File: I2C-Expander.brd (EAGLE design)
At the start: 106 x 100 mm, 81 parts, among them IC1 MCP23017SO, IC2 PCA9555D, Q0 P-FET, Q1 P-FET, Q10 P-FET, Q11 P-FET, Q12 P-FET, Q13 P-FET, Q14 P-FET, Q15 P-FET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

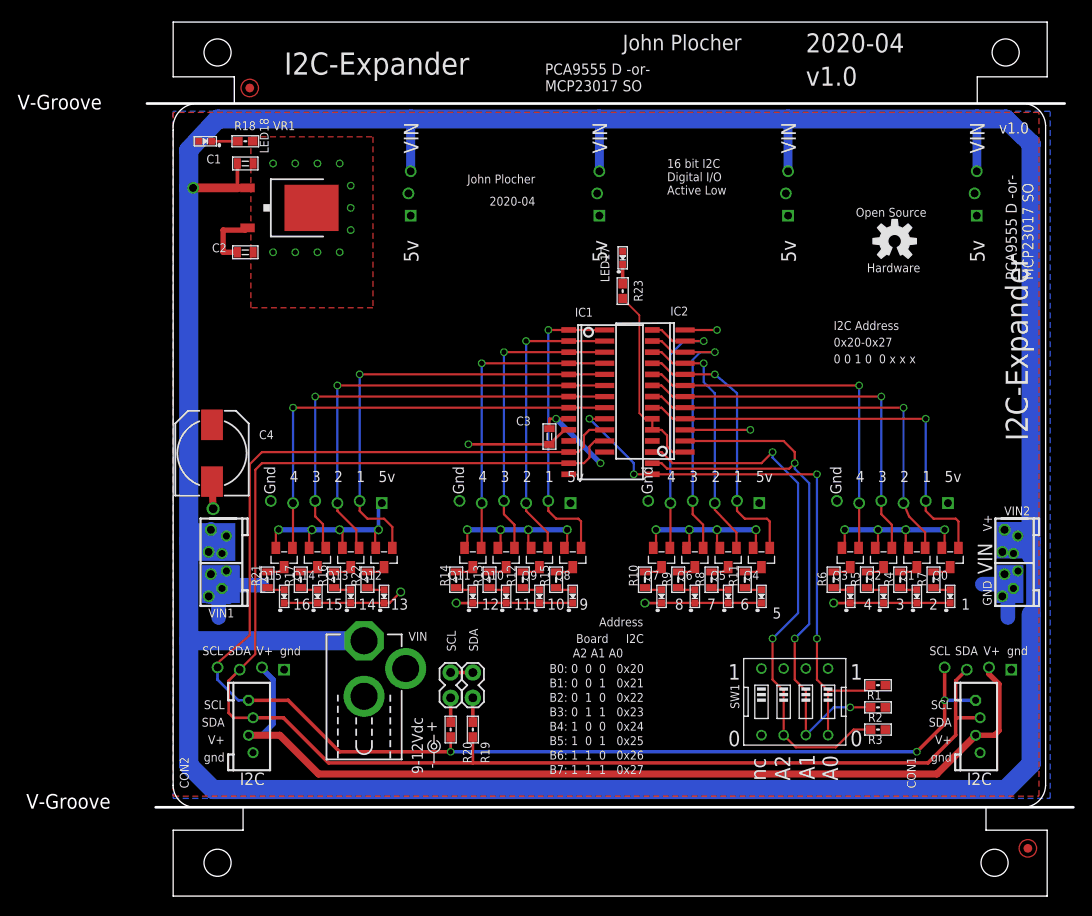
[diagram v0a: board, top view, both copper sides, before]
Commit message: FID placement & names
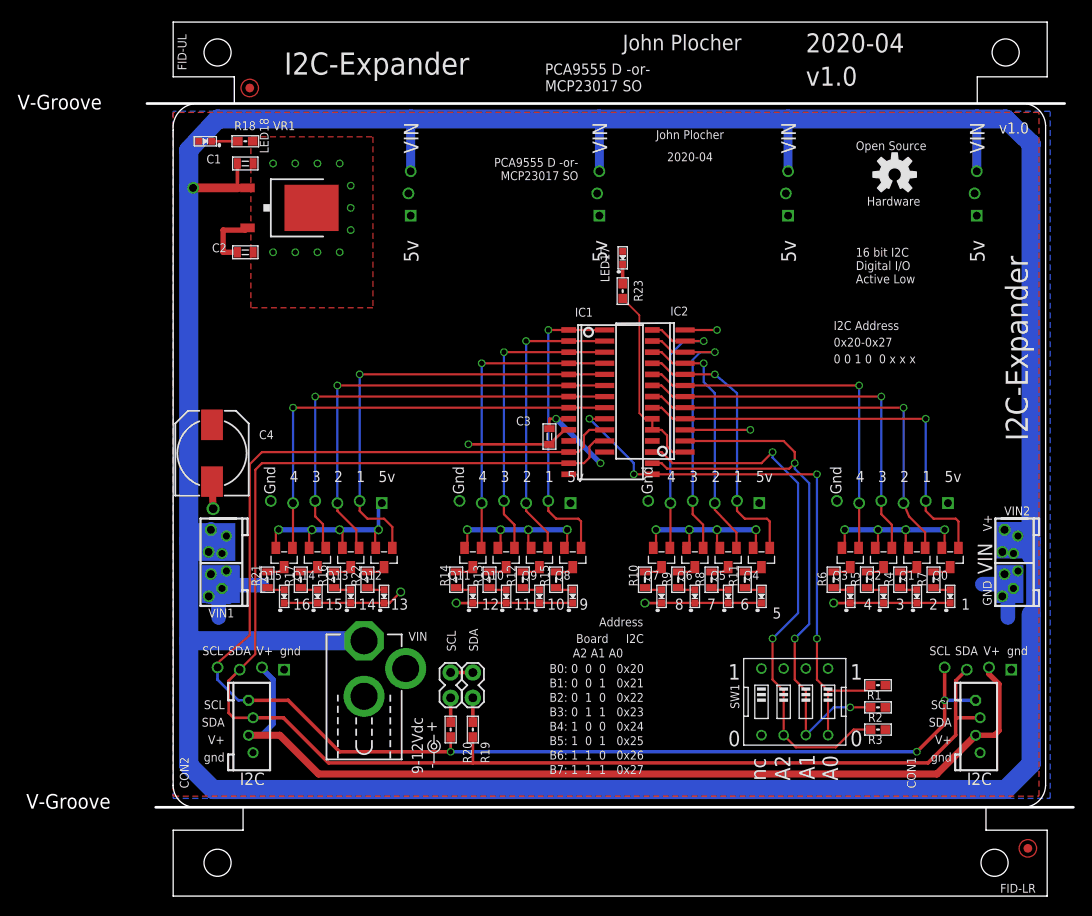
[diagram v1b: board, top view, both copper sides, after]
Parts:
- U$1, U$2, U$3: value CONNECTOR-IO4-IOBBARE -> CONNECTOR-IO4-IOBNOBSILK; device SPCoast:IO4-IOB -> SPCoast:IOB-IO4-NOBOTSILK
- U$4: value CONNECTOR-IO4-IOBBARE -> CONNECTOR-IO4-IOBFULL
- moved OSHW1 7.62 mm to (82.5, 82.5)
- renumbered FID1 to FID-UL, FID2 to FID-LR
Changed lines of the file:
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@@
 <setting verticaltext="up"/>
 </settings>
-<grid distance="50" unitdist="mil" unit="mil" style="dots" multiple="2" display="yes" altdistance="5" altunitdist="mil" altunit="mil"/>
+<grid distance="50" unitdist="mil" unit="mil" style="dots" multiple="2" display="yes" altdistance="25" altunitdist="mil" altunit="mil"/>
 <layers>
-<layer number="1" name="Top" color="4" fill="1" visible="no" active="yes"/>
-<layer number="16" name="Bottom" color="2" fill="1" visible="no" active="yes"/>
+<layer number="1" name="Top" color="4" fill="1" visible="yes" active="yes"/>
+<layer number="16" name="Bottom" color="2" fill="1" visible="yes" active="yes"/>
 <layer number="17" name="Pads" color="23" fill="1" visible="yes" active="yes"/>
 <layer number="18" name="Vias" color="29" fill="1" visible="yes" active="yes"/>
-<layer number="19" name="Unrouted" color="6" fill="1" visible="no" active="yes"/>
+<layer number="19" name="Unrouted" color="6" fill="1" visible="yes" active="yes"/>
 <layer number="20" name="Dimension" color="15" fill="1" visible="yes" active="yes"/>
 <layer number="21" name="tPlace" color="19" fill="1" visible="yes" active="yes"/>
 <layer number="22" name="bPlace" color="17" fill="1" visible="no" active="yes"/>
-<layer number="23" name="tOrigins" color="30" fill="1" visible="no" active="yes"/>
+<layer number="23" name="tOrigins" color="30" fill="1" visible="yes" active="yes"/>
 <layer number="24" name="bOrigins" color="15" fill="1" visible="no" active="yes"/>
-<layer number="25" name="tNames" color="63" fill="1" visible="no" active="yes"/>
+<layer number="25" name="tNames" color="63" fill="1" visible="yes" active="yes"/>
 <layer number="26" name="bNames" color="34" fill="1" visible="no" active="yes"/>
 <layer number="27" name="tValues" color="56" fill="1" visible="yes" active="yes"/>
@@
 <layer number="42" name="bRestrict" color="3" fill="10" visible="no" active="yes"/>
 <layer number="43" name="vRestrict" color="2" fill="10" visible="no" active="yes"/>
-<layer number="44" name="Drills" color="16" fill="1" visible="no" active="yes"/>
-<layer number="45" name="Holes" color="35" fill="1" visible="no" active="yes"/>
-<layer number="46" name="Milling" color="35" fill="1" visible="no" active="yes"/>
-<layer number="47" name="Measures" color="21" fill="1" visible="no" active="yes"/>
+<layer number="44" name="Drills" color="16" fill="1" visible="yes" active="yes"/>
+<layer number="45" name="Holes" color="35" fill="1" visible="yes" active="yes"/>
+<layer number="46" name="Milling" color="35" fill="1" visible="yes" active="yes"/>
+<layer number="47" name="Measures" color="21" fill="1" visible="yes" active="yes"/>
 <layer number="48" name="Document" color="57" fill="1" visible="yes" active="yes"/>
-<layer number="49" name="Reference" color="48" fill="1" visible="no" active="yes"/>
+<layer number="49" name="Reference" color="48" fill="1" visible="yes" active="yes"/>
 <layer number="50" name="dxf" color="7" fill="1" visible="no" active="yes"/>
 <layer number="51" name="tDocu" color="24" fill="1" visible="yes" active="yes"/>
@@
 <layer number="98" name="Guide" color="6" fill="1" visible="no" active="no"/>
 <layer number="99" name="Anatomie" color="7" fill="1" visible="no" active="no"/>
-<layer number="101" name="Hidden" color="57" fill="4" visible="no" active="yes"/>
+<layer number="101" name="Hidden" color="57" fill="4" visible="yes" active="yes"/>
 <layer number="2" name="Route2" color="1" fill="3" visible="no" active="no"/>
 <layer number="3" name="Route3" color="4" fill="3" visible="no" active="no"/>
@@
 <text x="72.39" y="96.52" size="2.1844" layer="21" font="vector" ratio="10">2020-04</text>
 <text x="97.79" y="46.99" size="2.1844" layer="21" font="vector" ratio="15" rot="R90">&gt;DRAWING_NAME </text>
-<text x="36.195" y="78.994" size="1.016" layer="21" font="vector" ratio="10">2020-04</text>
+<text x="56.515" y="84.074" size="1.016" layer="21" font="vector" ratio="10">2020-04</text>
 <text x="94.488" y="87.249" size="1.27" layer="21" font="vector" ratio="10">v1.0</text>
 <text x="90.17" y="32.766" size="1.27" layer="21">1</text>
@@
 <text x="63.5" y="24.765" size="1.778" layer="21" font="vector" ratio="10">1</text>
 <text x="67.818" y="13.208" size="1.778" layer="21" font="vector" ratio="10" rot="R90">nc</text>
-<text x="33.655" y="81.534" size="1.016" layer="21" font="vector" ratio="10">John Plocher</text>
-<text x="79.375" y="71.374" size="1.016" layer="21" font="vector" ratio="10">Hardware</text>
+<text x="55.245" y="86.614" size="1.016" layer="21" font="vector" ratio="10">John Plocher</text>
+<text x="79.375" y="78.994" size="1.016" layer="21" font="vector" ratio="10">Hardware</text>
 <text x="106.045" y="26.67" size="1.016" layer="47" font="vector" ratio="10" rot="R90">"</text>
 <text x="51.435" y="96.774" size="1.778" layer="21" font="vector" ratio="10">John Plocher</text>
-<text x="78.105" y="77.724" size="1.016" layer="21" font="vector" ratio="10">Open Source</text>
-<text x="56.515" y="80.264" size="1.016" layer="21" font="vector" ratio="10">16 bit I2C
+<text x="78.105" y="85.344" size="1.016" layer="21" font="vector" ratio="10">Open Source</text>
+<text x="78.105" y="70.104" size="1.016" layer="21" font="vector" ratio="10">16 bit I2C
 Digital I/O
 Active Low</text>
@@
 <wire x1="97.679" y1="8.001" x2="101.362" y2="13.081" width="2.54" layer="52"/>
 <wire x1="101.87" y1="19.431" x2="0.016" y2="82.169" width="1.778" layer="52"/>
-<text x="98.425" y="70.485" size="1.27" layer="21" font="vector" ratio="13" rot="R90">PCA9555 D -or-
+<text x="46.355" y="84.455" size="1.016" layer="21" font="vector" ratio="13" rot="R180">PCA9555 D -or-
 MCP23017 SO</text>
 <text x="42.545" y="92.075" size="1.27" layer="21" font="vector" ratio="13">PCA9555 D -or-
@@
 <elements>
 <element name="BOARD1" library="SPCoast" package="BOARD-DINRAIL-3.17IN-IOB" value="BOARD80X100-IOB" x="0" y="0" smashed="yes"/>
-<element name="FID1" library="SPCoast" package="FIDUCIAL_1MM" value="FIDUCIAL" x="8.763" y="92.456" smashed="yes"/>
-<element name="FID2" library="SPCoast" package="FIDUCIAL_1MM" value="FIDUCIAL" x="97.79" y="5.461" smashed="yes"/>
-<element name="OSHW1" library="SPCoast" package="OSHW-LOGO-M" value="DOC-OSHW-LOGO-M" x="82.55" y="74.93" smashed="yes"/>
+<element name="FID-UL" library="SPCoast" package="FIDUCIAL_1MM" value="FIDUCIAL" x="8.763" y="92.456" smashed="yes">
+<attribute name="NAME" x="1.524" y="94.488" size="1.016" layer="25" rot="R90"/>
+</element>
+<element name="FID-LR" library="SPCoast" package="FIDUCIAL_1MM" value="FIDUCIAL" x="97.79" y="5.461" smashed="yes">
+<attribute name="NAME" x="94.615" y="0.381" size="1.016" layer="25"/>
+</element>
+<element name="OSHW1" library="SPCoast" package="OSHW-LOGO-M" value="DOC-OSHW-LOGO-M" x="82.55" y="82.55" smashed="yes"/>
 <element name="IC1" library="SPCoast" package="SO28W" value="MCP23017SO" x="50.038" y="57.15" smashed="yes" rot="R270">
 <attribute name="MF" value="MICROCHIP" x="50.038" y="57.15" size="1.778" layer="27" font="vector" ratio="10" rot="R270" display="off"/>
@@
 <attribute name="VALUE" x="73.406" y="36.957" size="1.016" layer="27" ratio="10" rot="R180"/>
 </element>
-<element name="U$1" library="SPCoast" package="IO4-IOB" value="CONNECTOR-IO4-IOBBARE" x="73.66" y="90.17" smashed="yes" rot="R270"/>
-<element name="U$2" library="SPCoast" package="IO4-IOB" value="CONNECTOR-IO4-IOBBARE" x="52.07" y="90.17" smashed="yes" rot="R270"/>
-<element name="U$3" library="SPCoast" package="IO4-IOB" value="CONNECTOR-IO4-IOBBARE" x="30.48" y="90.17" smashed="yes" rot="R270"/>
-<element name="U$4" library="SPCoast" package="IO4-IOB" value="CONNECTOR-IO4-IOBBARE" x="8.89" y="90.17" smashed="yes" rot="R270"/>
+<element name="U$1" library="SPCoast" package="IOB-IO4-NOBOTSILK" value="CONNECTOR-IO4-IOBNOBSILK" x="73.66" y="90.17" smashed="yes" rot="R270"/>
+<element name="U$2" library="SPCoast" package="IOB-IO4-NOBOTSILK" value="CONNECTOR-IO4-IOBNOBSILK" x="52.07" y="90.17" smashed="yes" rot="R270"/>
+<element name="U$3" library="SPCoast" package="IOB-IO4-NOBOTSILK" value="CONNECTOR-IO4-IOBNOBSILK" x="30.48" y="90.17" smashed="yes" rot="R270"/>
+<element name="U$4" library="SPCoast" package="IO4-IOB" value="CONNECTOR-IO4-IOBFULL" x="8.89" y="90.17" smashed="yes" rot="R270"/>
 <element name="LED8" library="SPCoast" package="0603-LED" value="Y" x="67.31" y="34.29" smashed="yes" rot="R90">
 <attribute name="VALUE" x="73.152" y="34.036" size="1.016" layer="27" ratio="10" rot="R180"/>
